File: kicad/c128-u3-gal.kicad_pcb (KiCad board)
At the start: 2 copper layers, 56.5 x 27.3 mm, 5 parts, among them J1 Conn_02x04_Row_Letter_Last, J2 Conn_01x02, J3 Conn_01x04, U1 74LS138, U2 GAL20V10

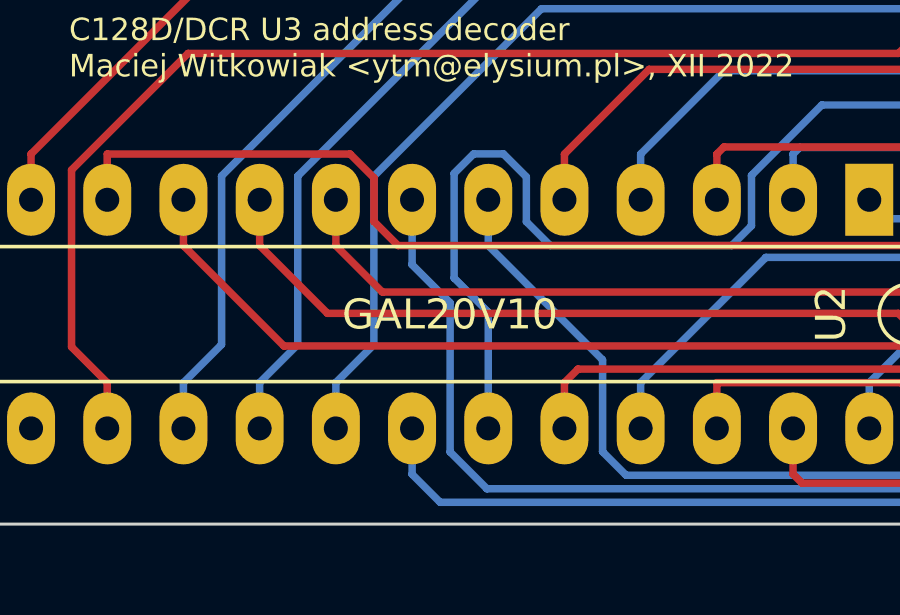
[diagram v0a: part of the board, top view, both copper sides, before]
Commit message: correct GAL device name to GAL22V10
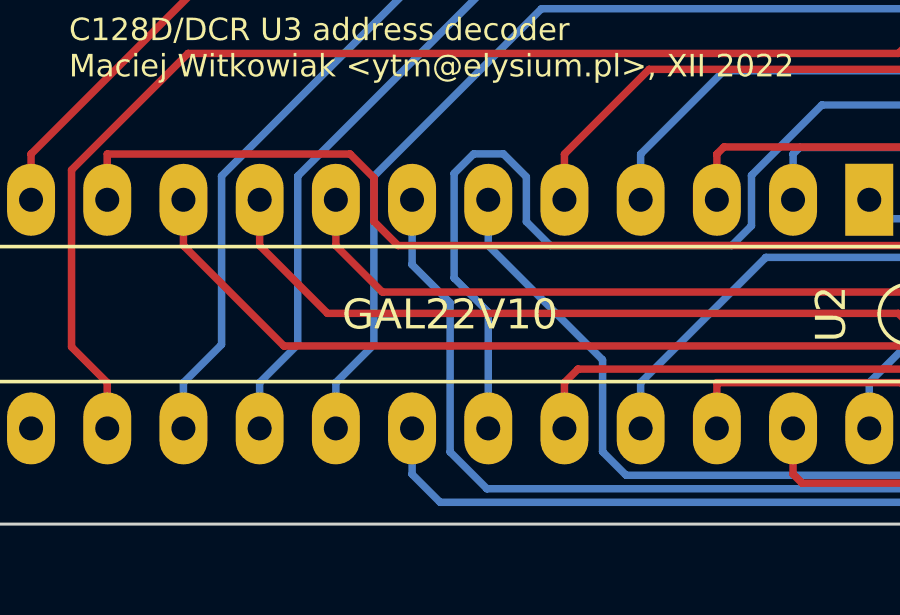
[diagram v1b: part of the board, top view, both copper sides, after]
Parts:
- U2: value GAL20V10 -> GAL22V10
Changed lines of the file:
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@@
       (effects (font (size 1 1) (thickness 0.15)))
     )
-    (fp_text value "GAL20V10" (at 3.825 13.975) (layer "F.SilkS")
+    (fp_text value "GAL22V10" (at 3.825 13.975) (layer "F.SilkS")
       (effects (font (size 1 1) (thickness 0.15)))
     )
